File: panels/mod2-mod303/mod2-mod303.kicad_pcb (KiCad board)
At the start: 2 copper layers, 19.8 x 128.5 mm, 0 parts

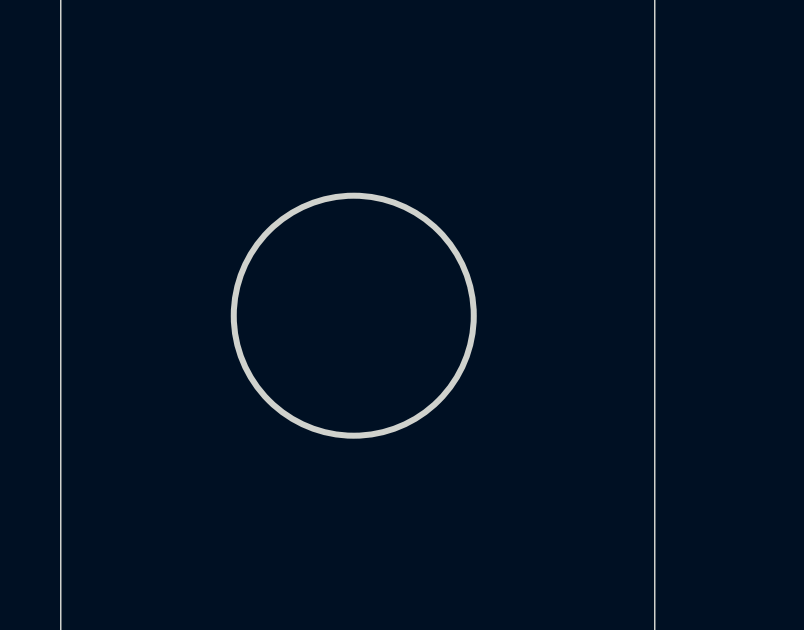
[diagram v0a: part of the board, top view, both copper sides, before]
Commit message: move vcvrack, update faceplates
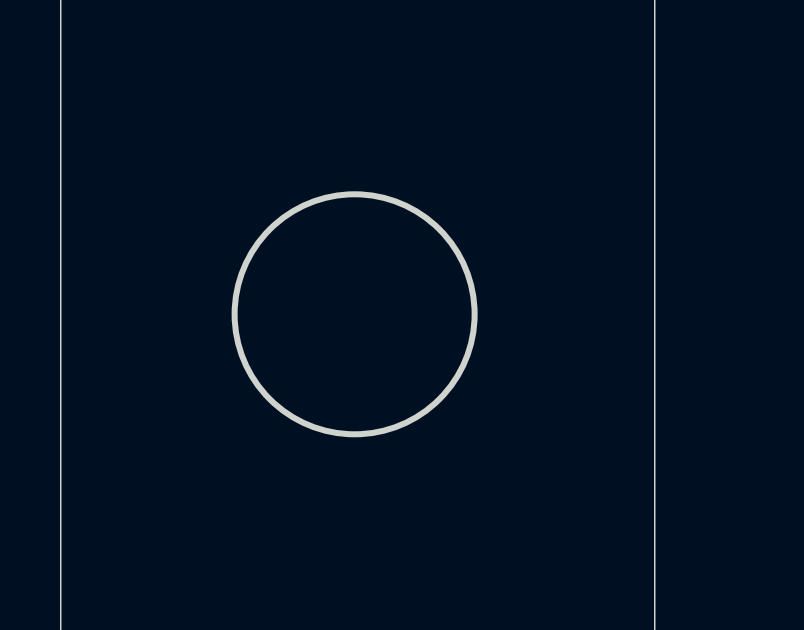
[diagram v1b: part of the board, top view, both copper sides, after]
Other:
- board text added: "16"
- board text added: "8"
- board text added: "RND"
- board text added: "Transpose"
- board text added: "mode select"
- board text added: "step / acc"
- board text added: "tap = scale dbl = wav long = regen"
- board text added: "| ACID 303 |"
- board text removed: "MOD303"
- board text removed: "Trans"
- board text removed: "scale"
- board text removed: "step"
